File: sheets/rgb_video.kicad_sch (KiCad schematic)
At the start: 51 parts, among them CN3 DIN-8, U32 CXA1145P

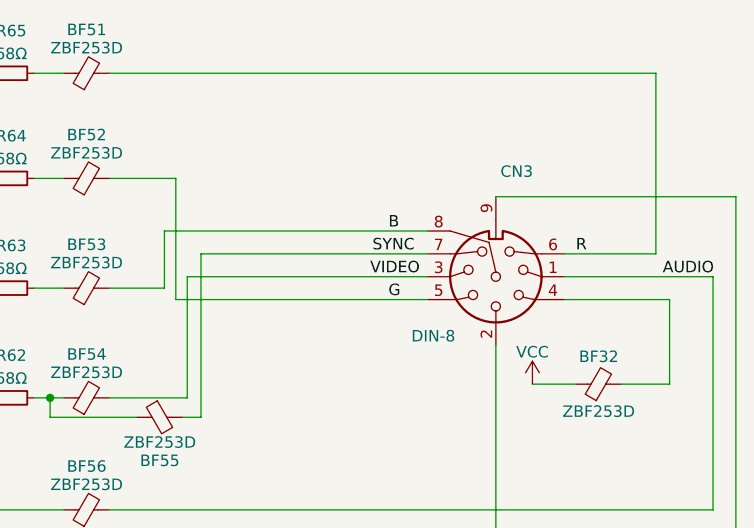
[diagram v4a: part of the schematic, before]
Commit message: RENAME SYNC TO CSYNC
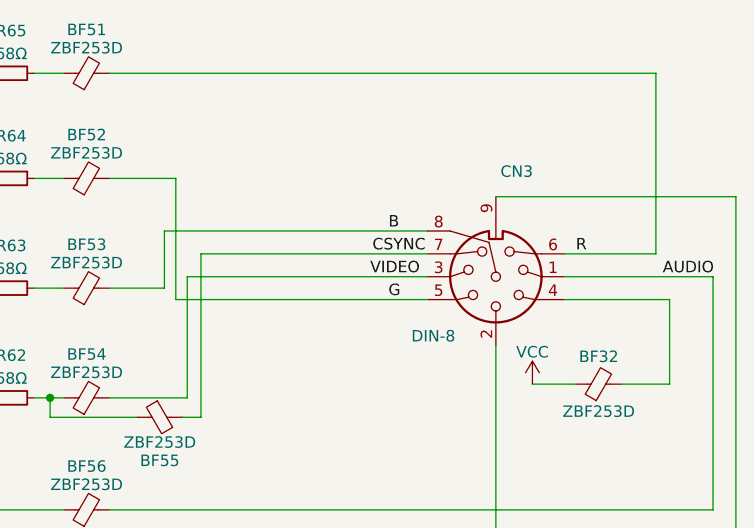
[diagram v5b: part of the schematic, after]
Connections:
- net SYNC: no longer BF55.2, CN3.7
- new net CSYNC: BF55.2, CN3.7
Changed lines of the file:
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@@
     (effects (font (size 1.27 1.27)) (justify left bottom))
   )
-  (label "SYNC" (at 308.61 96.774 0)
+  (label "CSYNC" (at 308.61 96.774 0)
     (effects (font (size 1.27 1.27)) (justify left bottom))
   )

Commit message: Sync Footprints from Nightly
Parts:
- C26, C29, C30, C31, C33, C42, C43, C60, C66: footprint 1_NeoGeoLibrary:CAP1-5mm -> 1_NeoGeoLibrary:CAP3-5mm
- C32, C34, C41: footprint 1_NeoGeoLibrary:CAP1-5mm -> 1_NeoGeoLibrary:CAP2-2.5mm
- C36, C37, C38, C39: footprint 1_NeoGeoLibrary:CAP3-5mm -> 1_NeoGeoLibrary:CAP1-5mm
- L1, L2: footprint 1_NeoGeoLibrary:Resistor1-5mm -> 1_NeoGeoLibrary:Inductor
- NTSC1, PAL2: footprint Resistor_THT:R_Axial_DIN0204_L3.6mm_D1.6mm_P5.08mm_Vertical -> 1_NeoGeoLibrary:PAL
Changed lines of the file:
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@@
       (effects (font (size 1.27 1.27)) (justify right))
     )
-    (property "Footprint" "1_NeoGeoLibrary:CAP1-5mm" (id 2) (at 167.386 179.324 0)
+    (property "Footprint" "1_NeoGeoLibrary:CAP2-2.5mm" (id 2) (at 167.386 179.324 0)
       (effects (font (size 1.27 1.27)) hide)
     )
@@
     (property "Reference" "C33" (id 0) (at 276.86 209.55 0))
     (property "Value" "100pF" (id 1) (at 276.86 211.582 0))
-    (property "Footprint" "1_NeoGeoLibrary:CAP1-5mm" (id 2) (at 271.526 210.312 0)
+    (property "Footprint" "1_NeoGeoLibrary:CAP3-5mm" (id 2) (at 271.526 210.312 0)
       (effects (font (size 1.27 1.27)) hide)
     )
@@
     (property "Reference" "C66" (id 0) (at 266.446 172.72 90))
     (property "Value" "1nF" (id 1) (at 266.446 170.688 90))
-    (property "Footprint" "1_NeoGeoLibrary:CAP1-5mm" (id 2) (at 266.446 168.148 0)
+    (property "Footprint" "1_NeoGeoLibrary:CAP3-5mm" (id 2) (at 266.446 168.148 0)
       (effects (font (size 1.27 1.27)) hide)
     )
@@
     (property "Reference" "C29" (id 0) (at 277.114 150.114 90))
     (property "Value" "100p (82p)" (id 1) (at 277.114 152.146 90))
-    (property "Footprint" "1_NeoGeoLibrary:CAP1-5mm" (id 2) (at 277.114 154.686 0)
+    (property "Footprint" "1_NeoGeoLibrary:CAP3-5mm" (id 2) (at 277.114 154.686 0)
       (effects (font (size 1.27 1.27)) hide)
     )
@@
     (property "Reference" "C34" (id 0) (at 253.492 120.904 90))
     (property "Value" "10uF" (id 1) (at 253.492 122.682 90))
-    (property "Footprint" "1_NeoGeoLibrary:CAP1-5mm" (id 2) (at 253.492 125.222 0)
+    (property "Footprint" "1_NeoGeoLibrary:CAP2-2.5mm" (id 2) (at 253.492 125.222 0)
       (effects (font (size 1.27 1.27)) hide)
     )
@@
     (property "Reference" "PAL2" (id 0) (at 168.402 143.256 0))
     (property "Value" "0" (id 1) (at 166.624 145.542 0))
-    (property "Footprint" "Resistor_THT:R_Axial_DIN0204_L3.6mm_D1.6mm_P5.08mm_Vertical" (id 2) (at 164.846 144.399 0)
+    (property "Footprint" "1_NeoGeoLibrary:PAL" (id 2) (at 164.846 144.399 0)
       (effects (font (size 1.27 1.27)) hide)
     )
@@
     (property "Reference" "L2" (id 0) (at 258.826 179.07 90))
     (property "Value" "47uH" (id 1) (at 258.826 181.61 90))
-    (property "Footprint" "1_NeoGeoLibrary:Resistor1-5mm" (id 2) (at 258.826 183.896 0)
+    (property "Footprint" "1_NeoGeoLibrary:Inductor" (id 2) (at 258.826 183.896 0)
       (effects (font (size 1.27 1.27)) hide)
     )
@@
     (property "Reference" "C60" (id 0) (at 157.734 183.388 0))
     (property "Value" "100pF" (id 1) (at 157.734 185.42 0))
-    (property "Footprint" "1_NeoGeoLibrary:CAP1-5mm" (id 2) (at 152.4 184.15 0)
+    (property "Footprint" "1_NeoGeoLibrary:CAP3-5mm" (id 2) (at 152.4 184.15 0)
       (effects (font (size 1.27 1.27)) hide)
     )
@@
     (property "Reference" "NTSC1" (id 0) (at 169.164 133.096 0))
     (property "Value" "0" (id 1) (at 166.878 135.382 0))
-    (property "Footprint" "Resistor_THT:R_Axial_DIN0204_L3.6mm_D1.6mm_P5.08mm_Vertical" (id 2) (at 164.846 134.112 0)
+    (property "Footprint" "1_NeoGeoLibrary:PAL" (id 2) (at 164.846 134.112 0)
       (effects (font (size 1.27 1.27)) hide)
     )
@@
     (property "Reference" "L1" (id 0) (at 287.274 149.86 90))
     (property "Value" "47uH" (id 1) (at 287.274 152.4 90))
-    (property "Footprint" "1_NeoGeoLibrary:Resistor1-5mm" (id 2) (at 287.274 154.686 0)
+    (property "Footprint" "1_NeoGeoLibrary:Inductor" (id 2) (at 287.274 154.686 0)
       (effects (font (size 1.27 1.27)) hide)
     )
@@
     (property "Reference" "C42" (id 0) (at 141.478 165.608 90))
     (property "Value" "100pF" (id 1) (at 141.478 167.64 90))
-    (property "Footprint" "1_NeoGeoLibrary:CAP1-5mm" (id 2) (at 141.478 170.688 0)
+    (property "Footprint" "1_NeoGeoLibrary:CAP3-5mm" (id 2) (at 141.478 170.688 0)
       (effects (font (size 1.27 1.27)) hide)
     )
@@
     (property "Reference" "C43" (id 0) (at 297.434 167.894 0))
     (property "Value" "47pF" (id 1) (at 297.434 169.926 0))
-    (property "Footprint" "1_NeoGeoLibrary:CAP1-5mm" (id 2) (at 292.1 168.656 0)
+    (property "Footprint" "1_NeoGeoLibrary:CAP3-5mm" (id 2) (at 292.1 168.656 0)
       (effects (font (size 1.27 1.27)) hide)
     )
@@
     (property "Reference" "C30" (id 0) (at 266.446 159.766 90))
     (property "Value" "0.01uF" (id 1) (at 266.446 161.798 90))
-    (property "Footprint" "1_NeoGeoLibrary:CAP1-5mm" (id 2) (at 266.446 164.338 0)
+    (property "Footprint" "1_NeoGeoLibrary:CAP3-5mm" (id 2) (at 266.446 164.338 0)
       (effects (font (size 1.27 1.27)) hide)
     )
@@
       (effects (font (size 1.27 1.27)) (justify right))
     )
-    (property "Footprint" "1_NeoGeoLibrary:CAP1-5mm" (id 2) (at 237.998 210.312 0)
+    (property "Footprint" "1_NeoGeoLibrary:CAP2-2.5mm" (id 2) (at 237.998 210.312 0)
       (effects (font (size 1.27 1.27)) hide)
     )
@@
     (property "Reference" "C39" (id 0) (at 253.492 108.458 90))
     (property "Value" "100uF/6.3v" (id 1) (at 253.492 110.236 90))
-    (property "Footprint" "1_NeoGeoLibrary:CAP3-5mm" (id 2) (at 253.492 112.776 0)
+    (property "Footprint" "1_NeoGeoLibrary:CAP1-5mm" (id 2) (at 253.492 112.776 0)
       (effects (font (size 1.27 1.27)) hide)
     )
@@
     (property "Reference" "C36" (id 0) (at 253.492 72.39 90))
     (property "Value" "100uF/6.3v" (id 1) (at 253.492 74.168 90))
-    (property "Footprint" "1_NeoGeoLibrary:CAP3-5mm" (id 2) (at 253.492 76.708 0)
+    (property "Footprint" "1_NeoGeoLibrary:CAP1-5mm" (id 2) (at 253.492 76.708 0)
       (effects (font (size 1.27 1.27)) hide)
     )
@@
     (property "Reference" "C38" (id 0) (at 253.492 96.266 90))
     (property "Value" "100uF/6.3v" (id 1) (at 253.492 98.044 90))
-    (property "Footprint" "1_NeoGeoLibrary:CAP3-5mm" (id 2) (at 253.492 100.584 0)
+    (property "Footprint" "1_NeoGeoLibrary:CAP1-5mm" (id 2) (at 253.492 100.584 0)
       (effects (font (size 1.27 1.27)) hide)
     )
@@
     (property "Reference" "C37" (id 0) (at 253.492 84.074 90))
     (property "Value" "100uF/6.3v" (id 1) (at 253.492 85.852 90))
-    (property "Footprint" "1_NeoGeoLibrary:CAP3-5mm" (id 2) (at 253.492 88.392 0)
+    (property "Footprint" "1_NeoGeoLibrary:CAP1-5mm" (id 2) (at 253.492 88.392 0)
       (effects (font (size 1.27 1.27)) hide)
     )
@@
     (property "Reference" "C31" (id 0) (at 259.334 189.23 90))
     (property "Value" "39pF (30pF)" (id 1) (at 259.334 191.262 90))
-    (property "Footprint" "1_NeoGeoLibrary:CAP1-5mm" (id 2) (at 259.334 193.802 0)
+    (property "Footprint" "1_NeoGeoLibrary:CAP3-5mm" (id 2) (at 259.334 193.802 0)
       (effects (font (size 1.27 1.27)) hide)
     )
@@
     (property "Reference" "C26" (id 0) (at 101.092 93.472 90))
     (property "Value" "0.1uF" (id 1) (at 101.092 95.504 90))
-    (property "Footprint" "1_NeoGeoLibrary:CAP1-5mm" (id 2) (at 101.092 98.552 0)
-      (effects (font (size 1.27 1.27)) hide)
-    )
+    (property "Footprint" "1_NeoGeoLibrary:CAP3-5mm" (id 2) (at 101.092 98.552 0)
+      (effects (font (size 1.27 1.27)) hide)
+    )

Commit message: Merged From Stable
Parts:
- L1: footprint 1_NeoGeoLibrary:Inductor -> 1_NeoGeoLibrary:L1
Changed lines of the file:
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@@
     (property "Reference" "L1" (id 0) (at 287.274 149.86 90))
     (property "Value" "47uH" (id 1) (at 287.274 152.4 90))
-    (property "Footprint" "1_NeoGeoLibrary:Inductor" (id 2) (at 287.274 154.686 0)
+    (property "Footprint" "1_NeoGeoLibrary:L1" (id 2) (at 287.274 154.686 0)
       (effects (font (size 1.27 1.27)) hide)
     )

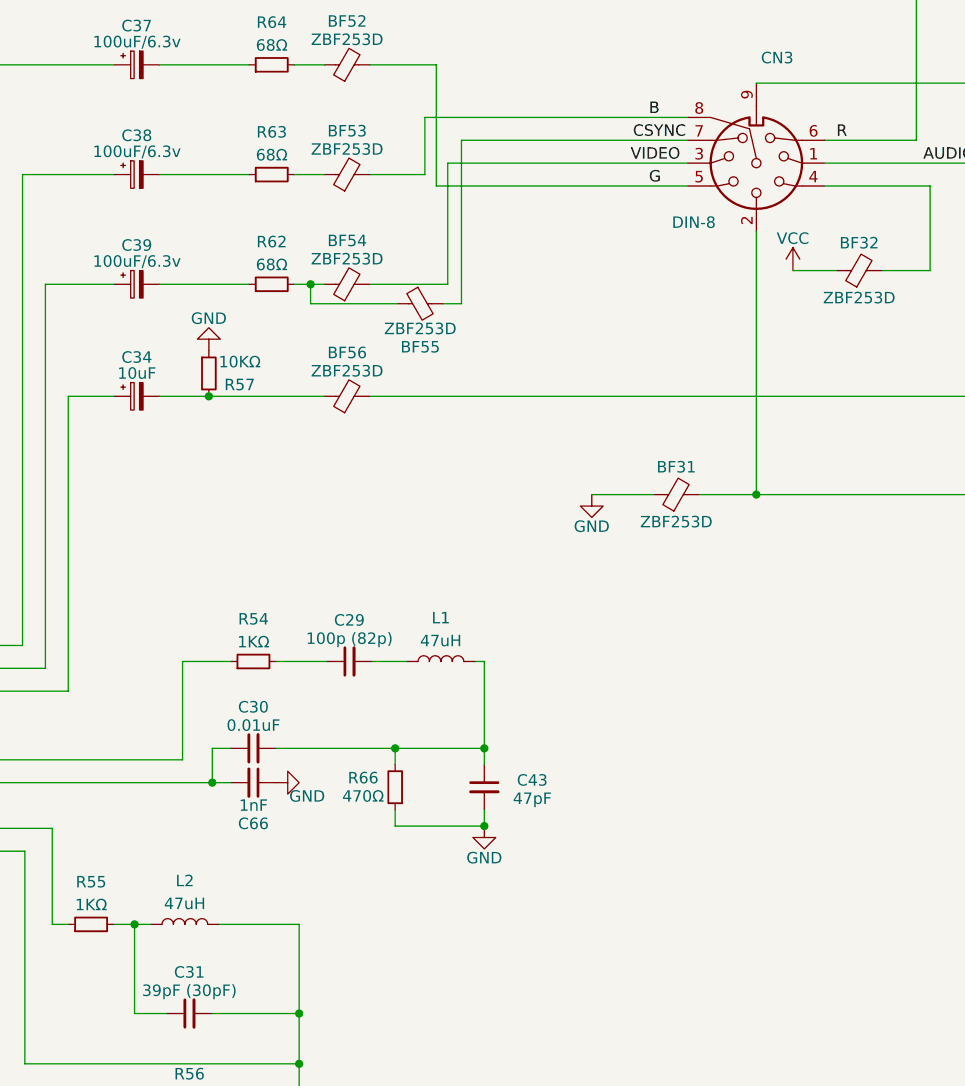
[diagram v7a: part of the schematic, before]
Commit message: Upgrade Schematics to Kicad 7.0
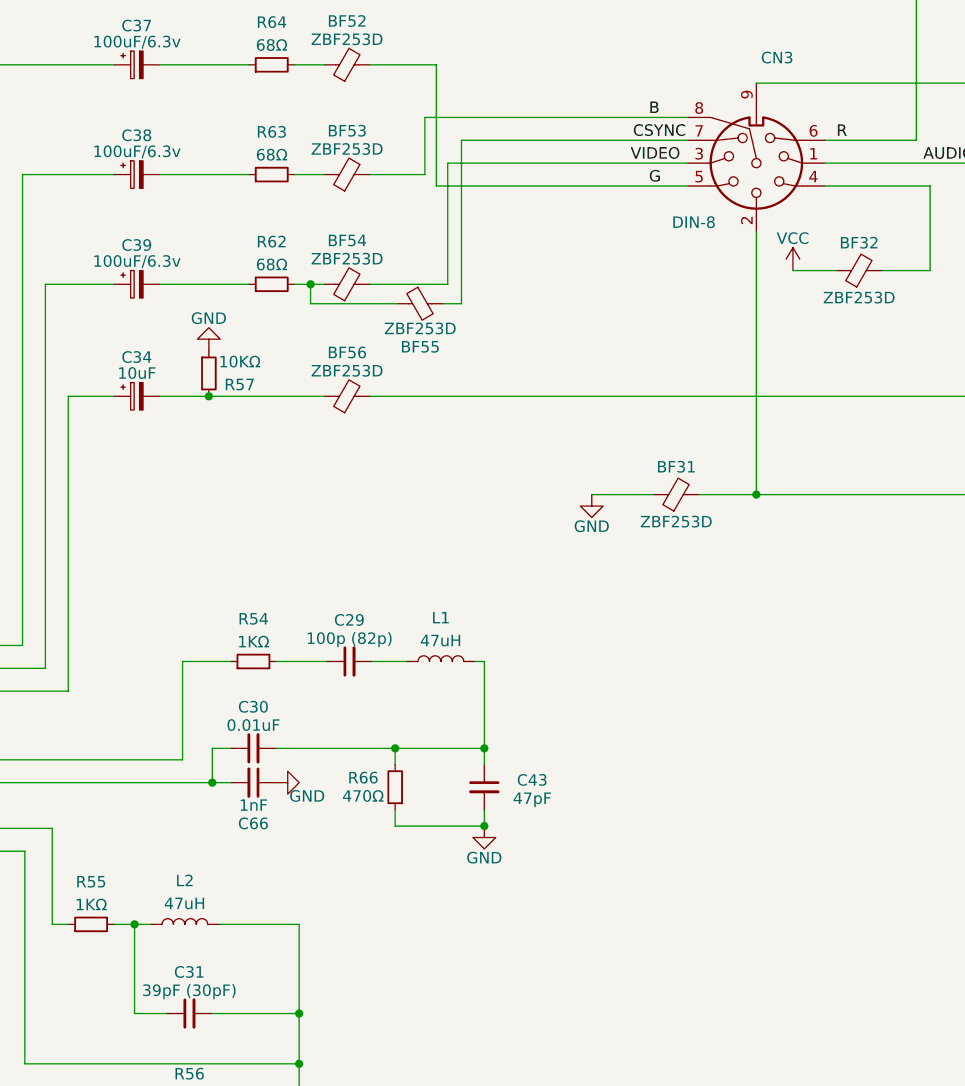
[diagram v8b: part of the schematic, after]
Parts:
- CN3: footprint Connector_Dsub:DSUB-9_Female_Horizontal_P2.77x2.84mm_EdgePinOffset4.94mm_Housed_MountingHolesOffset7.48mm -> 1_NeoGeoLibrary:CN3
